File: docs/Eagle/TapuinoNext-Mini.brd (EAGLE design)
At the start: 74.9 x 39 mm, 10 parts, among them U1 ESP32-DEVKITC-38

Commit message: Changed rotary wiring back to original to match stripboard
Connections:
- net BTN_PREV/ROTB: now also BUTTONS.2, U1.8; no longer BUTTONS.3, U1.7
- net BTN_SEL/ROTARY: now also BUTTONS.3, U1.7; no longer BUTTONS.2, U1.8
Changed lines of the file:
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@@
 </signal>
 <signal name="BTN_PREV/ROTB">
+<contactref element="U1" pad="8"/>
+<contactref element="BUTTONS" pad="2"/>
+<wire x1="50.8" y1="40.64" x2="50.81" y2="40.63" width="0.1524" layer="16"/>
+<wire x1="50.8" y1="40.64" x2="50.81" y2="40.63" width="0.1524" layer="1"/>
+<wire x1="50.81" y1="40.63" x2="50.81" y2="36.82" width="0.1524" layer="1"/>
+</signal>
+<signal name="BTN_SEL/ROTARY">
+<contactref element="U1" pad="7"/>
 <contactref element="BUTTONS" pad="3"/>
-<contactref element="U1" pad="7"/>
+<wire x1="53.34" y1="40.64" x2="53.35" y2="40.63" width="0.1524" layer="16"/>
 <wire x1="53.34" y1="40.64" x2="53.35" y2="40.63" width="0.1524" layer="1"/>
 <wire x1="53.35" y1="40.63" x2="53.35" y2="36.82" width="0.1524" layer="1"/>
 </signal>
-<signal name="BTN_SEL/ROTARY">
-<contactref element="BUTTONS" pad="2"/>
-<contactref element="U1" pad="8"/>
-<wire x1="50.8" y1="40.64" x2="50.81" y2="40.63" width="0.1524" layer="1"/>
-<wire x1="50.81" y1="40.63" x2="50.81" y2="36.82" width="0.1524" layer="1"/>
-</signal>
 <signal name="BTN_NEXT/ROTA">

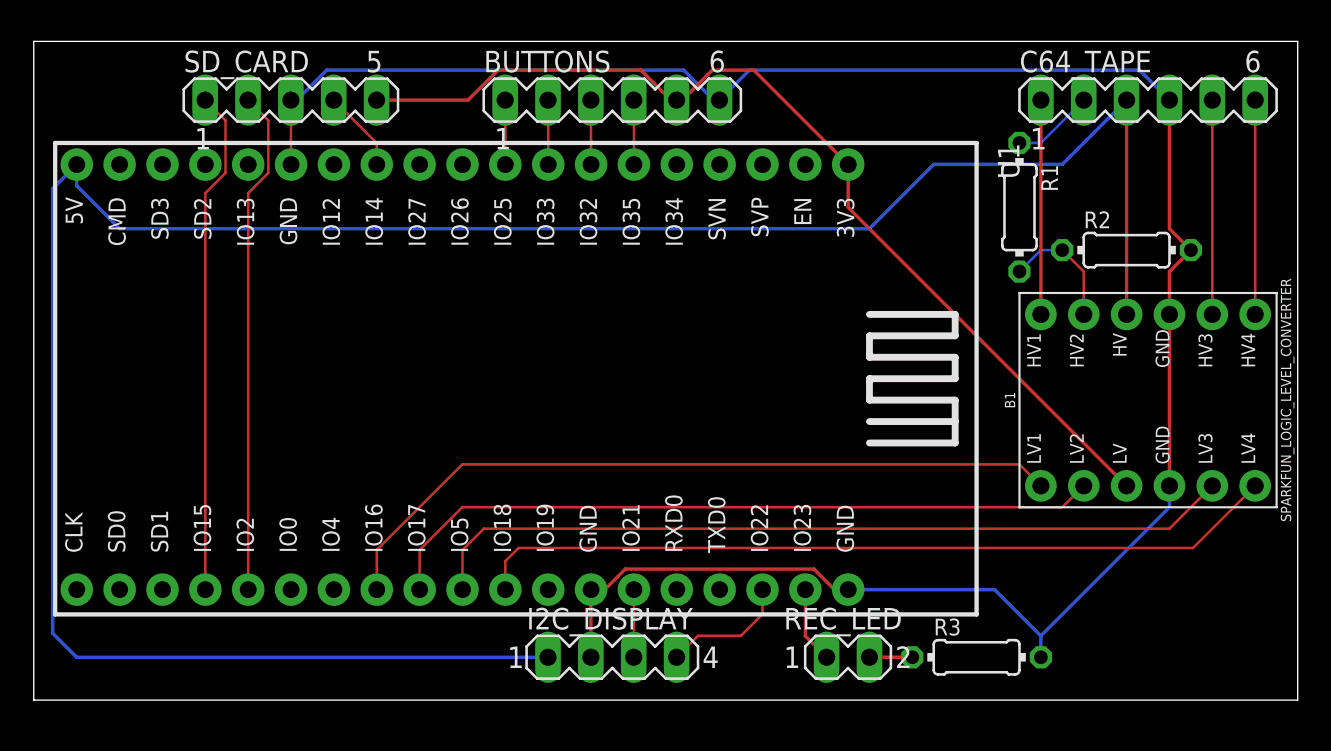
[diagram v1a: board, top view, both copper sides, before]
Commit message: Fixed pinout across all of the schematics, hopefully for the last time
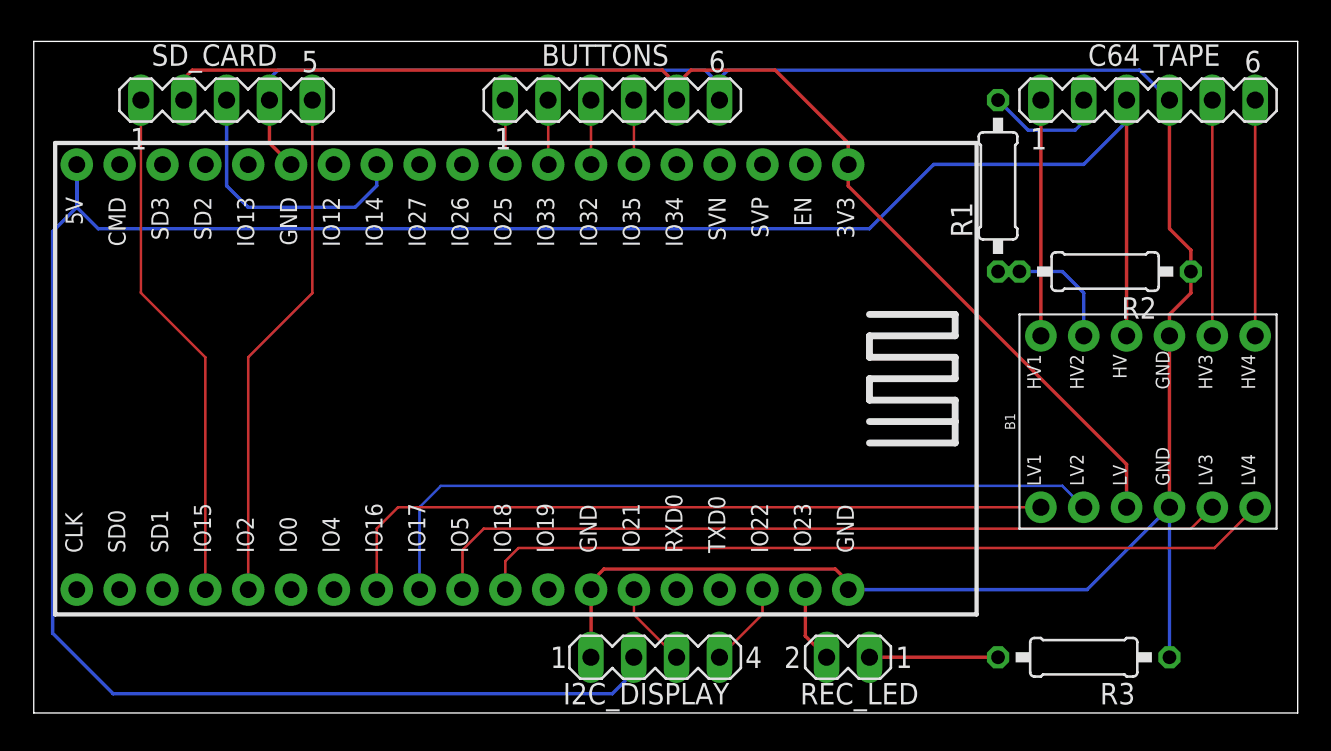
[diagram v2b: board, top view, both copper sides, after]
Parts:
- R1, R2, R3: device rcl:0204/7 -> rcl:0207/10
- moved R3 6.35 mm to (82.5, 7.62), turned to 180 degrees
- moved SD_CARD 3.81 mm to (31.8, 40.6)
- moved I2C_DISPLAY 2.54 mm to (57.1, 7.62)
- moved R2 1.80 mm to (83.8, 30.5), turned to 180 degrees
- moved R1 1.80 mm to (77.5, 35.6), turned to 90 degrees
- moved B1 1.27 mm to (86.4, 21.6)
- turned REC_LED to 180 degrees
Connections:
- removed net N$2: R3.1, REC_LED.2
- new net N$1: R3.2, REC_LED.1
- net 3V3: now also SD_CARD.2; no longer SD_CARD.5
- net C64+5V: now also I2C_DISPLAY.2; no longer I2C_DISPLAY.1
- net C64MOTOR: now also R1.2; no longer R1.1
- net C64MOTOR_5V: now also R1.1, R2.2; no longer R1.2, R2.1
- net GND: now also I2C_DISPLAY.1, R2.1, R3.1, SD_CARD.4; no longer I2C_DISPLAY.2, R2.2, R3.2, SD_CARD.3
- net REC_LED: now also REC_LED.2; no longer REC_LED.1
- net SDCLK: now also SD_CARD.3; no longer SD_CARD.4
- net SDDO: now also SD_CARD.5; no longer SD_CARD.2
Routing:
- net 3V3: track 58.4 -> 72.7 mm
- net SDCLK: track 4.88 -> 16.3 mm
- net C64+5V: track 138.7 -> 148.9 mm
- net GND: track 128.9 -> 138.6 mm
- net N$1: track 0.00 -> 7.62 mm
- net N$2: track 2.54 -> 0.00 mm
- net SCL: track 7.61 -> 5.07 mm
- net C64MOTOR: track 4.86 -> 7.30 mm
- net MOTOR: track 43.3 -> 45.3 mm
- net C64WRITE: track 12.7 -> 14.0 mm
- net C64SENSE: track 12.7 -> 14.0 mm
- net C64READ: track 12.7 -> 14.0 mm
- net SDA: track 4.01 -> 5.06 mm
- net SENSE: track 44.3 -> 43.5 mm
- net C64MOTOR_5V: track 7.40 -> 8.15 mm
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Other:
- board size 74.9 x 39 mm -> 74.9 x 39.8 mm
- board text added: "(c) 2021 sweetlilmre Minimum Reference Board"
- board text removed: "TapuinoNext (c) 2021 sweetlilmre Minimum Reference Board"
